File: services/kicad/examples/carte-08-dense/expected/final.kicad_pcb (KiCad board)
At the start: 4 copper layers, 125 x 95 mm, 56 parts, among them J1 IN_5V, J10 IO0, J11 IO1, J12 IO2, J13 IO3, J14 IO4, J2 SWD, U1 STM32F103C8T6, U2 AMS1117-3.3

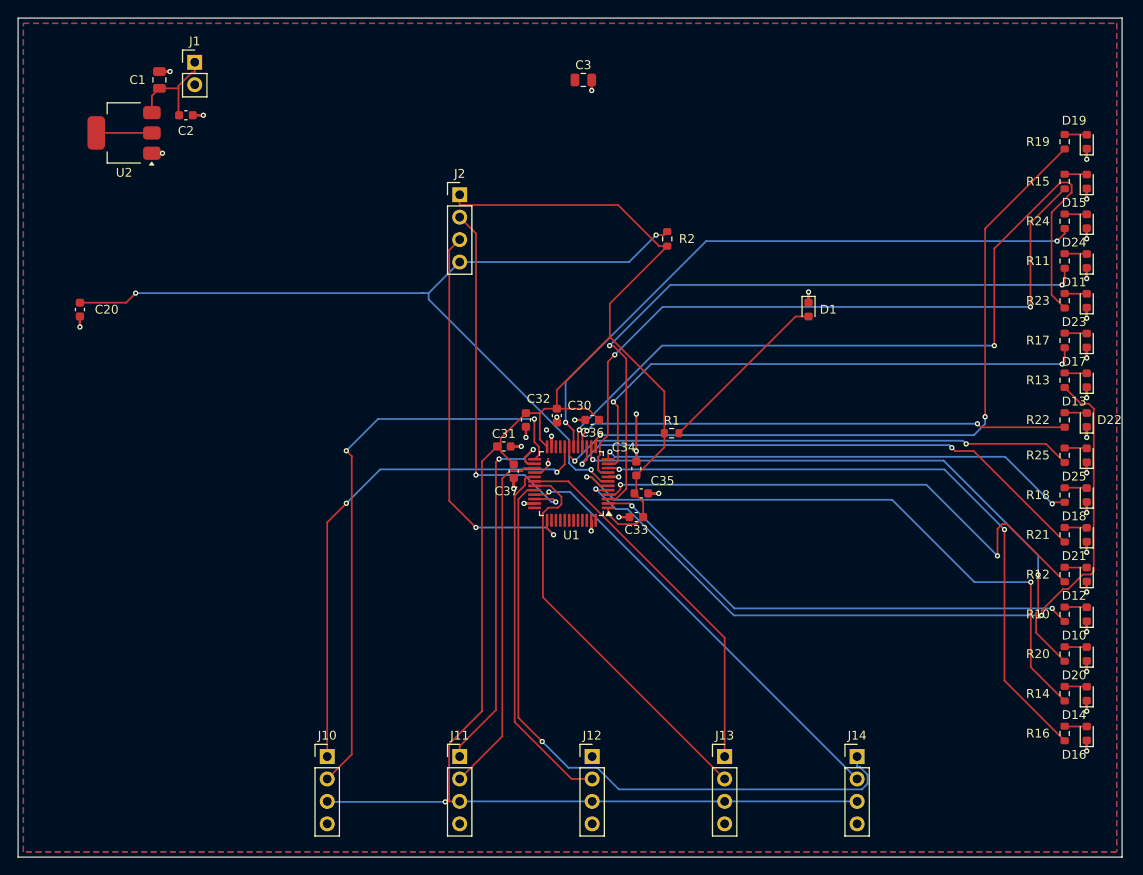
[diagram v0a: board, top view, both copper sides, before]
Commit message: fix(banc): le contour n etait JAMAIS resserre — dix cartes divisees par 2 a 4
Question de l utilisateur devant les rendus : « tu es satisfait de ce
placement ? ». Non, et la mesure lui donnait raison.

    carte-10 livree     140 x 105 mm = 14725 mm2
    son circuit          51 x  66 mm =  3366 mm2
    OCCUPATION                            23 %
    connecteurs                      56 a 75 mm du circuit
    fil de signal                      1230 mm  (VIN a lui seul 112 mm)

LA CAUSE : `run_pipeline.py` n envoyait pas `auto_size_board` a `/place/auto`.
Le resserrement du contour sur le placement existe depuis le 2026-09-13 et ne
s execute que si l appelant l autorise ; le defaut du modele est `False`.

C est le SEPTIEME levier de ce projet qui existe et que personne n appelle,
apres max_distance_mm, anchor_pin, WorkflowConfig.grid, constraints,
move_reference, bottom_up_placement et LocalRerouter.

⚠️ Et il etait INVISIBLE : la chaine de PRODUCTION passe bien le drapeau depuis
`handlePlacement`. Le banc mesurait donc un comportement que le produit n a
pas — l inverse exact de ce a quoi sert un banc.

MESURE APRES CORRECTION, meme circuit, meme graine :

    carte             demandee      REELLE        err  manq
    carte-01           25 x 20     20,1 x 14,6     0    0
    carte-02           55 x 40     34,9 x 25,4     0    0
    carte-03           50 x 35     26,1 x 20,1     0    0
    carte-04           60 x 45     36,6 x 27,2     0    0
    carte-05           70 x 50     43,6 x 32,6     0    0
    carte-06           80 x 60     48,5 x 36,4     0    0
    carte-07          110 x 80     53,2 x 38,8     0    0
    carte-08          125 x 95     56,4 x 44,1     0    0
    carte-09          130 x 100    57,3 x 45,2     0    0
    carte-10          140 x 105    61,0 x 45,8     0    0

Dix sur dix, 100 % route, aucune erreur, aucune connexion manquante. Sur
carte-10 : occupation 23 -> 56 %, fil de signal 1230 -> 652 mm, VIN 112 -> 45,5,
connecteurs 56-75 -> 23-35 mm.

ET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
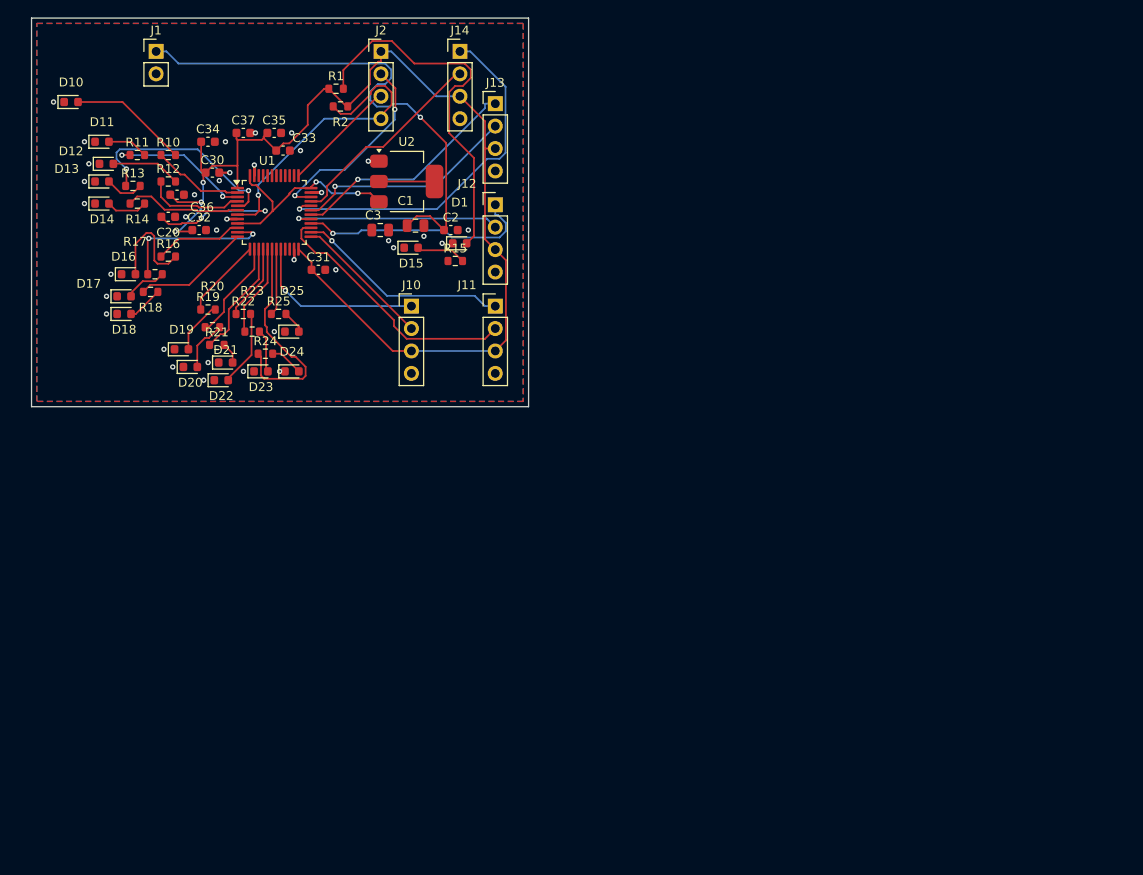
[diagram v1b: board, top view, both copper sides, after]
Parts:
- moved D10 128.8 mm to (92.0, 67.0), turned to 0 degrees
- moved D14 124.5 mm to (95.5, 78.5), turned to 0 degrees
- moved D12 120.3 mm to (96.0, 74.0), turned to 0 degrees
- moved D16 120.3 mm to (98.5, 86.5), turned to 0 degrees
- moved R14 118.8 mm to (99.5, 78.5), turned to 0 degrees
- moved R16 115.0 mm to (103.0, 84.5), turned to 0 degrees
- moved R10 114.0 mm to (103.0, 73.0), turned to 0 degrees
- moved D13 113.7 mm to (95.5, 76.0), turned to 0 degrees
- moved D11 112.3 mm to (95.5, 71.5), turned to 0 degrees
- moved D18 110.9 mm to (98.0, 91.0), turned to 0 degrees
- moved R12 110.8 mm to (103.0, 76.0), turned to 0 degrees
- moved D17 109.1 mm to (98.0, 89.0), turned to 0 degrees
- moved R13 107.8 mm to (99.0, 76.5), turned to 0 degrees
- moved D20 106.6 mm to (105.5, 97.0), turned to 0 degrees
- moved R18 106.0 mm to (101.0, 88.5), turned to 0 degrees
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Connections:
- U1 pad 36: Net-(U1-36) -> PWR_FLAG
- U1 pad 48: Net-(U1-48) -> PWR_FLAG
- U1 pad 9: IO_L5 -> PWR_FLAG
- U2 pad 3: VIN -> PWR_FLAG
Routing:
- net IO_L13: track 91.5 -> 10.5 mm, vias 2 -> 0
- net IO_L5: track 79.4 -> 0.00 mm, vias 2 -> 0
- net +3V3: track 204.1 -> 126.4 mm, vias 1 -> 3
- net GND: track 90.6 -> 15.6 mm, vias 36 -> 35
- net IO_L9: track 80.5 -> 9.15 mm, vias 2 -> 0
- net IO_L3: track 88.9 -> 24.0 mm
- net IO_L6: track 74.5 -> 10.0 mm, vias 2 -> 0
- net IO_L4: track 73.1 -> 13.2 mm, vias 2 -> 0
- net IO_L1: track 75.9 -> 16.1 mm
- net IO_L10: track 69.9 -> 11.4 mm, vias 2 -> 0
- net NRST: track 101.1 -> 48.3 mm
- net IO_L15: track 59.3 -> 7.58 mm, vias 2 -> 0
- net EXT0_2: track 66.3 -> 15.7 mm, vias 2 -> 0
- net IO_L2: track 61.8 -> 11.2 mm, vias 2 -> 0
- net IO_L11: track 62.4 -> 13.4 mm, vias 2 -> 0
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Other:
- board size 125 x 95 mm -> 56.3 x 44 mm
- copper layers 4 -> 2

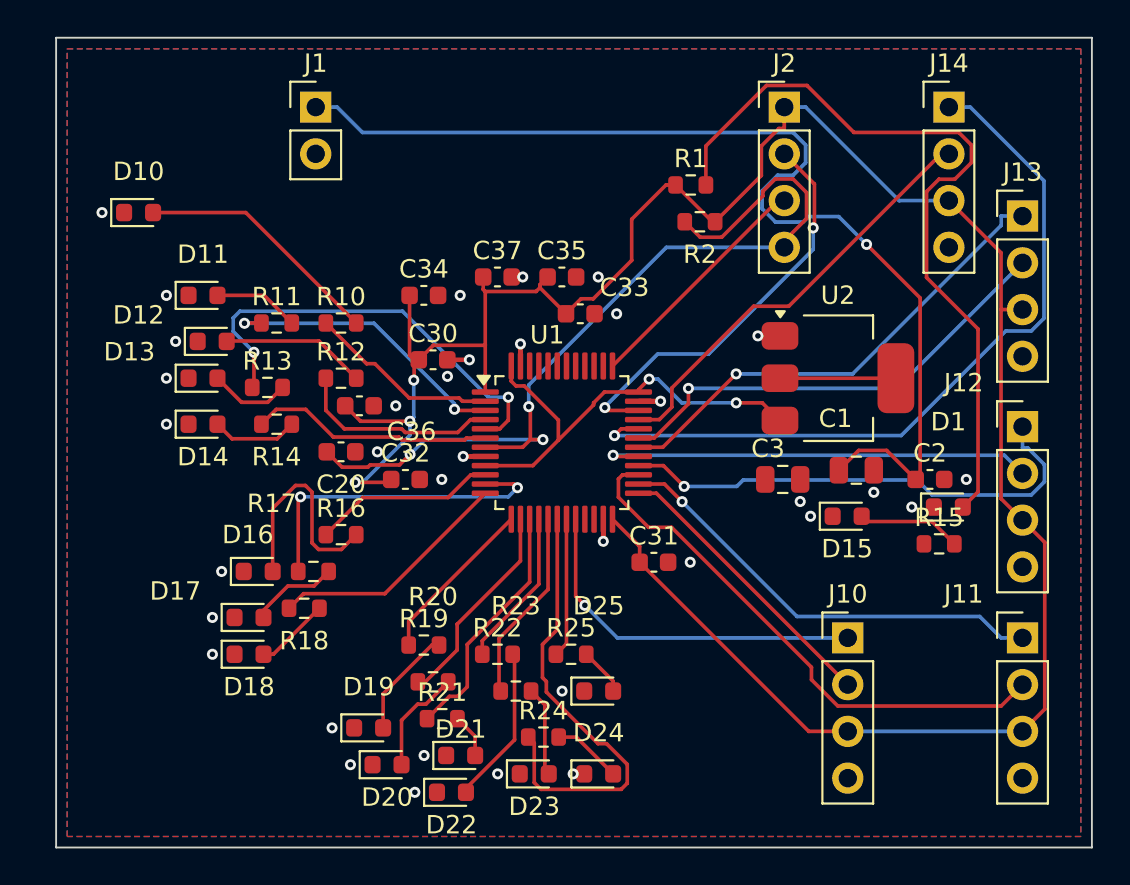
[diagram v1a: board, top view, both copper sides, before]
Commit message: feat(placement): les peripheriques se REPARTISSENT, ils ne s empilent plus
Question de l utilisateur devant le rendu : « c est quoi ce type de placement ? ».
Les composants s entassaient d un seul cote du boitier, etiquettes de
serigraphie l une sur l autre, trois quarts de la couronne vides.

TROIS CAUSES, toutes dans `_poser_les_peripheriques`, toutes la meme faute —
un angle unique pour tout un groupe :

  - les DIRECTS qui visent la meme broche (tous les decouplages d un rail,
    toutes les resistances d un meme signal) recevaient le MEME `angle_vers`
    et le meme rayon de depart ;
  - les SUIVEURS d un meme parent recevaient tous atan2(parent - centre) ;
  - les ISOLES partaient tous de l angle 0.0, c est-a-dire du meme point.

`le_long_du_rayon` ne s ecartait qu une fois la place prise : d ou la file.

REMEDE : `_ecart_en_eventail`. Le PREMIER de chaque groupe garde EXACTEMENT la
direction calculee — c est la topologie, on ne la perd pas pour faire joli — et
les suivants s ecartent symetriquement de 3 x `_PAS_ANGLE_DEG`.
Rien de deja pose ne bouge : seul l ANGLE DE DEPART de la recherche change, et
`le_long_du_rayon` reste seul juge de ce qui est libre.

BANC DES DIX CARTES, contour resserre ET peripheriques repartis :

    carte             demandee    livree         err  manq
    carte-01           25 x 20    20,1 x 13,6     0    0
    carte-02           55 x 40    34,9 x 25,2     0    0
    carte-03           50 x 35    27,6 x 19,9     0    0
    carte-04           60 x 45    36,6 x 29,8     0    0
    carte-05           70 x 50    40,0 x 32,6     0    0
    carte-06           80 x 60    46,5 x 36,4     0    0
    carte-07          110 x 80    47,7 x 38,8     0    0
    carte-08          125 x 95    57,4 x 44,1     0    0
    carte-09          130 x 100   57,8 x 45,2     0    0
    carte-10          140 x 105   59,0 x 45,8     0    0

Dix sur dix, 100 % route. carte-07 gagne 5,5 mm de largeur sur le passage
precedent, carte-06 deux, carte-10 deux. Sur ca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
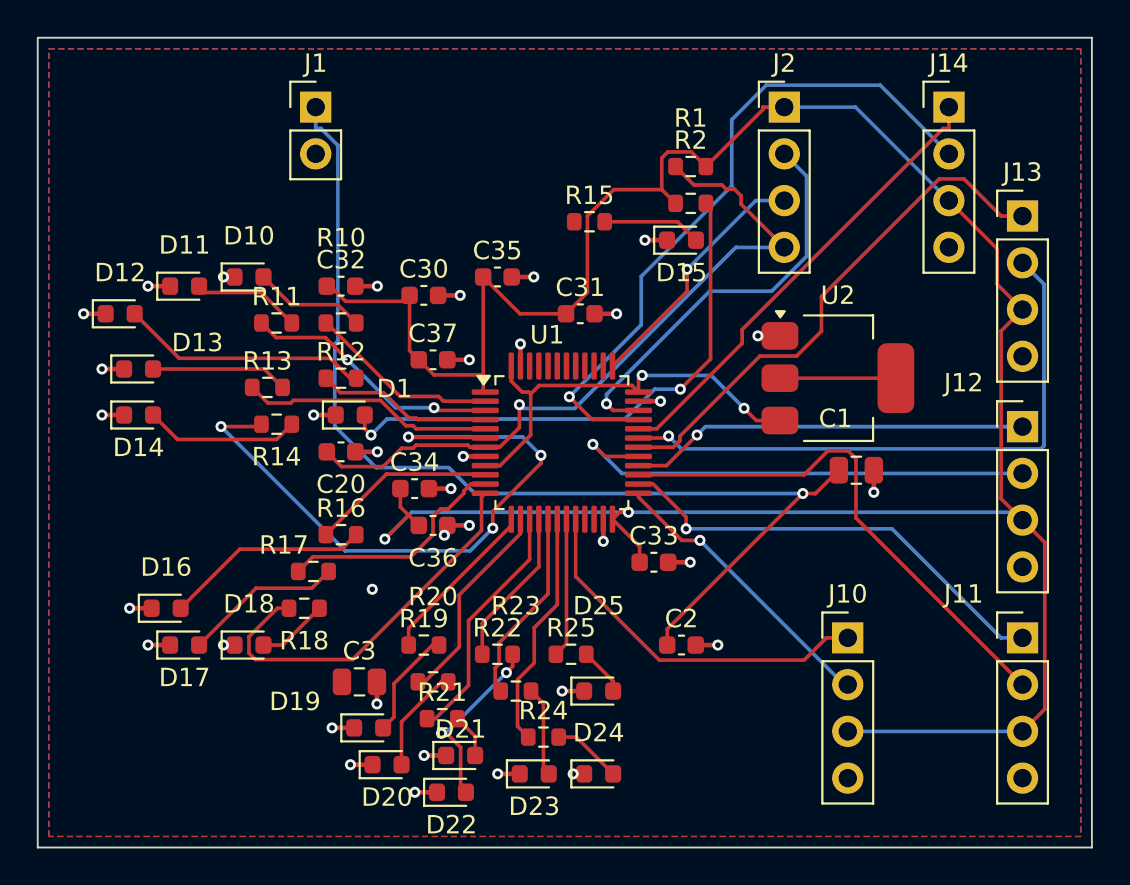
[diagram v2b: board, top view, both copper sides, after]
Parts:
- moved D1 32.9 mm to (103.5, 78.0)
- moved R15 25.8 mm to (116.5, 67.5)
- moved C3 25.5 mm to (104.0, 92.5)
- moved D15 17.5 mm to (121.5, 68.5)
- moved C2 16.2 mm to (121.5, 90.5)
- moved C31 14.1 mm to (116.0, 72.5)
- moved C33 14.1 mm to (120.0, 86.0)
- moved C32 11.1 mm to (103.0, 71.0)
- moved C34 10.5 mm to (107.0, 82.0)
- moved C36 7.63 mm to (108.0, 84.0)
- moved D10 6.95 mm to (98.0, 70.5)
- moved C37 5.70 mm to (108.0, 75.0)
- moved D16 5.39 mm to (93.5, 88.5)
- moved D12 5.22 mm to (91.0, 72.5)
- moved D17 3.81 mm to (94.5, 90.5)
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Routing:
- net IO_L4: track 13.2 -> 37.2 mm, vias 0 -> 4
- net GND: track 15.6 -> 39.0 mm, vias 35 -> 36
- net EXT4_1: track 41.7 -> 25.2 mm, vias 1 -> 0
- net +3V3: track 126.4 -> 142.4 mm, vias 3 -> 2
- net EXT4_2: track 23.5 -> 37.1 mm, vias 0 -> 1
- net LED_PWR: track 41.9 -> 30.0 mm, vias 0 -> 2
- net IO_L14: track 24.8 -> 13.0 mm
- net IO_L3: track 24.0 -> 13.7 mm, vias 2 -> 0
- net NRST: track 48.3 -> 39.1 mm, vias 3 -> 1
- net IO_L8: track 13.3 -> 21.5 mm
- net EXT3_2: track 25.3 -> 32.9 mm
- net LEDA0: track 13.5 -> 6.07 mm
- net LEDA2: track 7.88 -> 13.5 mm
- net EXT2_1: track 27.0 -> 21.7 mm
- net IO_L7: track 17.9 -> 12.8 mm, vias 2 -> 0
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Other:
- board size 56.3 x 44 mm -> 57.3 x 44 mm

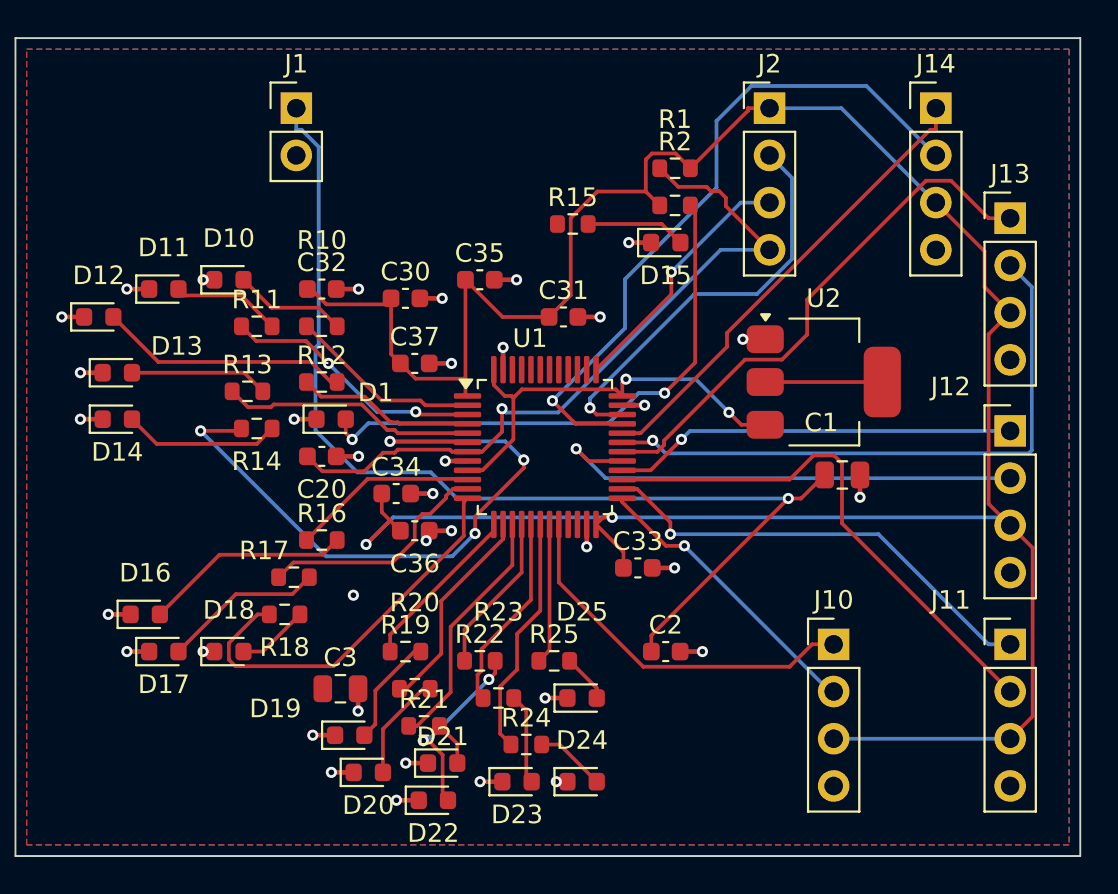
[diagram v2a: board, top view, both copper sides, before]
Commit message: docs(banc): les dix boards du banc du 2026-09-23, service corrige
Artefacts du banc dont le tableau est deja commite : les dix cartes a
100 % route, 0 erreur, 0 connexion manquante, chacune a la taille de son
circuit.

Co-Authored-By: Claude Opus 5 <noreply@anthropic.com>
Claude-Session: https://claude.ai/code/session_01TnMqm4La2CxQHHB5K8aSSV
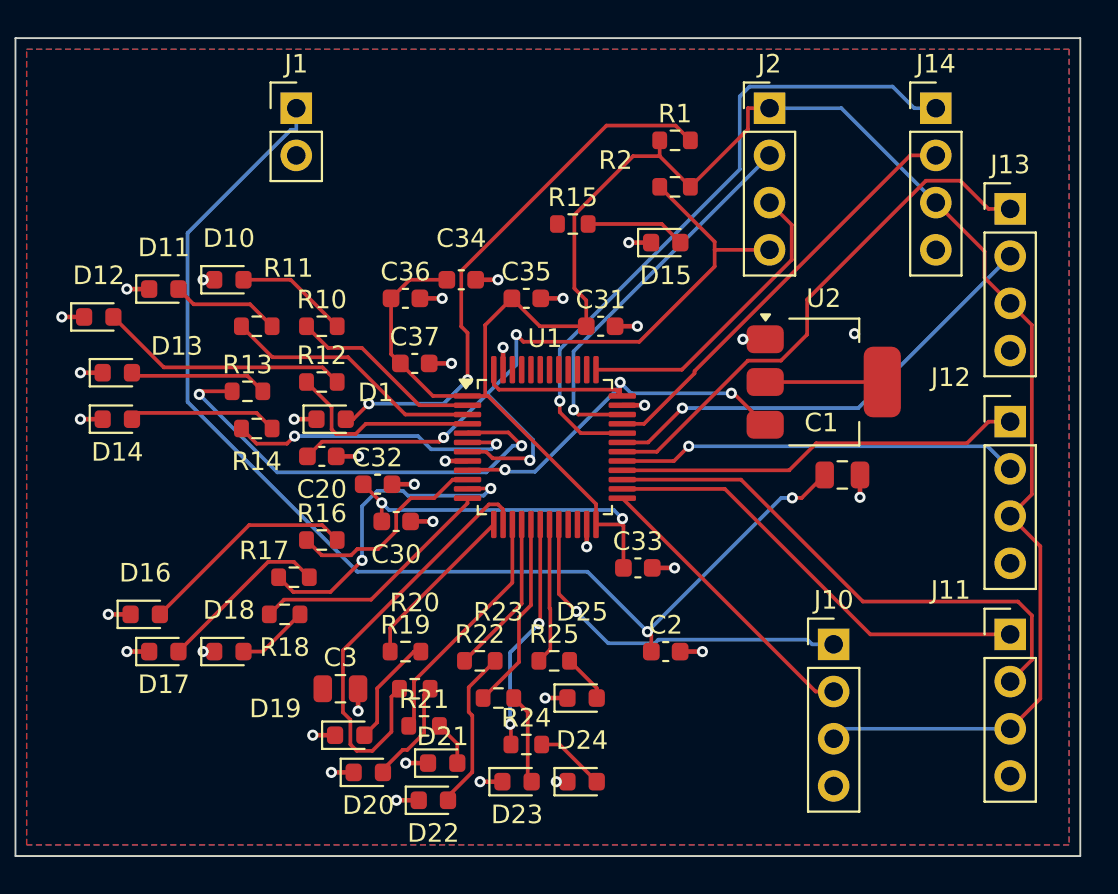
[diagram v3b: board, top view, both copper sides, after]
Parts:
- moved C36 12.5 mm to (107.5, 71.5)
- moved C34 12.0 mm to (110.5, 70.5)
- moved C30 12.0 mm to (107.0, 83.5)
- moved C32 10.9 mm to (106.0, 81.5)
- moved R1 3.50 mm to (122.0, 63.0)
- moved C35 2.69 mm to (114.0, 71.5)
- moved C31 2.06 mm to (118.0, 73.0)
- moved R2 1.00 mm to (122.0, 65.5)
- moved J11 0.53 mm to (140.0, 89.6)
- moved J12 0.50 mm to (140.0, 78.1)
- moved J13 0.50 mm to (140.0, 66.7)
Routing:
- net IO_L4: track 37.2 -> 16.2 mm, vias 4 -> 2
- net +3V3: track 142.4 -> 127.2 mm
- net EXT4_2: track 37.1 -> 22.9 mm, vias 1 -> 0
- net IO_L10: track 11.4 -> 23.3 mm
- net IO_L3: track 13.7 -> 24.7 mm, vias 0 -> 2
- net EXT4_1: track 25.2 -> 36.1 mm, vias 0 -> 1
- net IO_L8: track 21.5 -> 13.4 mm
- net EXT3_2: track 32.9 -> 25.0 mm
- net EXT2_2: track 26.7 -> 21.7 mm
- net NRST: track 39.1 -> 44.1 mm, vias 1 -> 3
- net PWR_FLAG: track 23.2 -> 27.8 mm, vias 2 -> 3
- net IO_L7: track 12.8 -> 17.2 mm, vias 0 -> 2
- net VIN: track 58.8 -> 62.4 mm, vias 1 -> 2
- net SWCLK: track 13.8 -> 16.5 mm, vias 1 -> 0
- net SWDIO: track 22.4 -> 20.8 mm
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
